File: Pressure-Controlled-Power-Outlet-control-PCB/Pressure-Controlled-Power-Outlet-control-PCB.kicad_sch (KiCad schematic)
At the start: 56 parts, among them J1 pressure sensor, J10 Conn_01x02_Pin, J2 1017514, J3 I2C0 Connector, J4 SPI1 Connector, J5 FanA 5V/12V, J6 FanB 5V/12V, J7 Conn_01x02_Pin, K1 T9GV5L24-24, K2 T9GV5L24-24, M1 Fan_4pin, M2 Fan_4pin, Q1 2N3906, Q2 IRF540N, Q3 IRF540N, Q4 2N3906, Q5 2N3904, Q6 2N3904, Q7 2N3904, Q8 2N3904, U1 Pico, U2 LM324, U3 LD1085V50, U4 LM1085-12

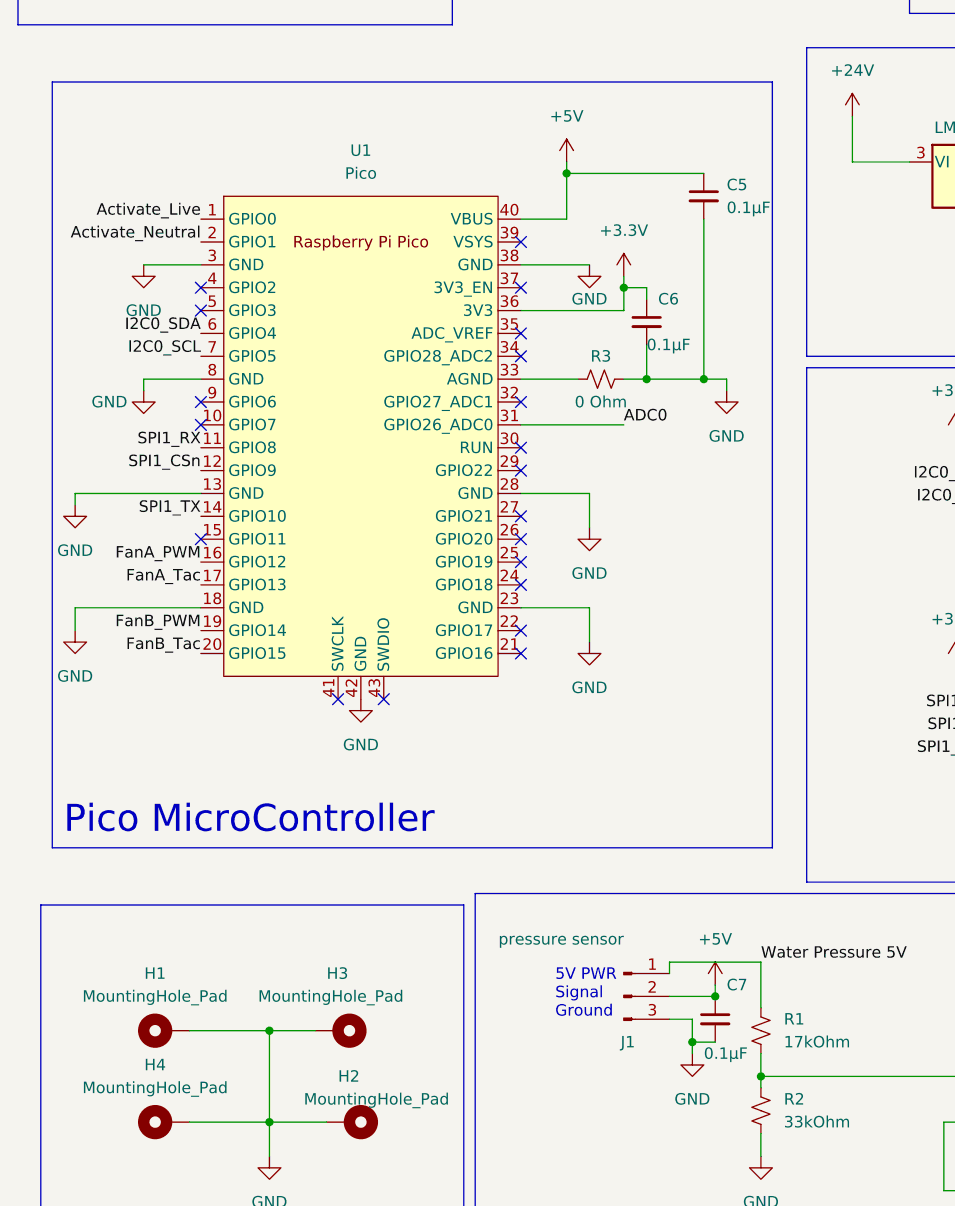
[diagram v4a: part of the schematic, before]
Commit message: created new updated PCB design that will fit the mount of the case
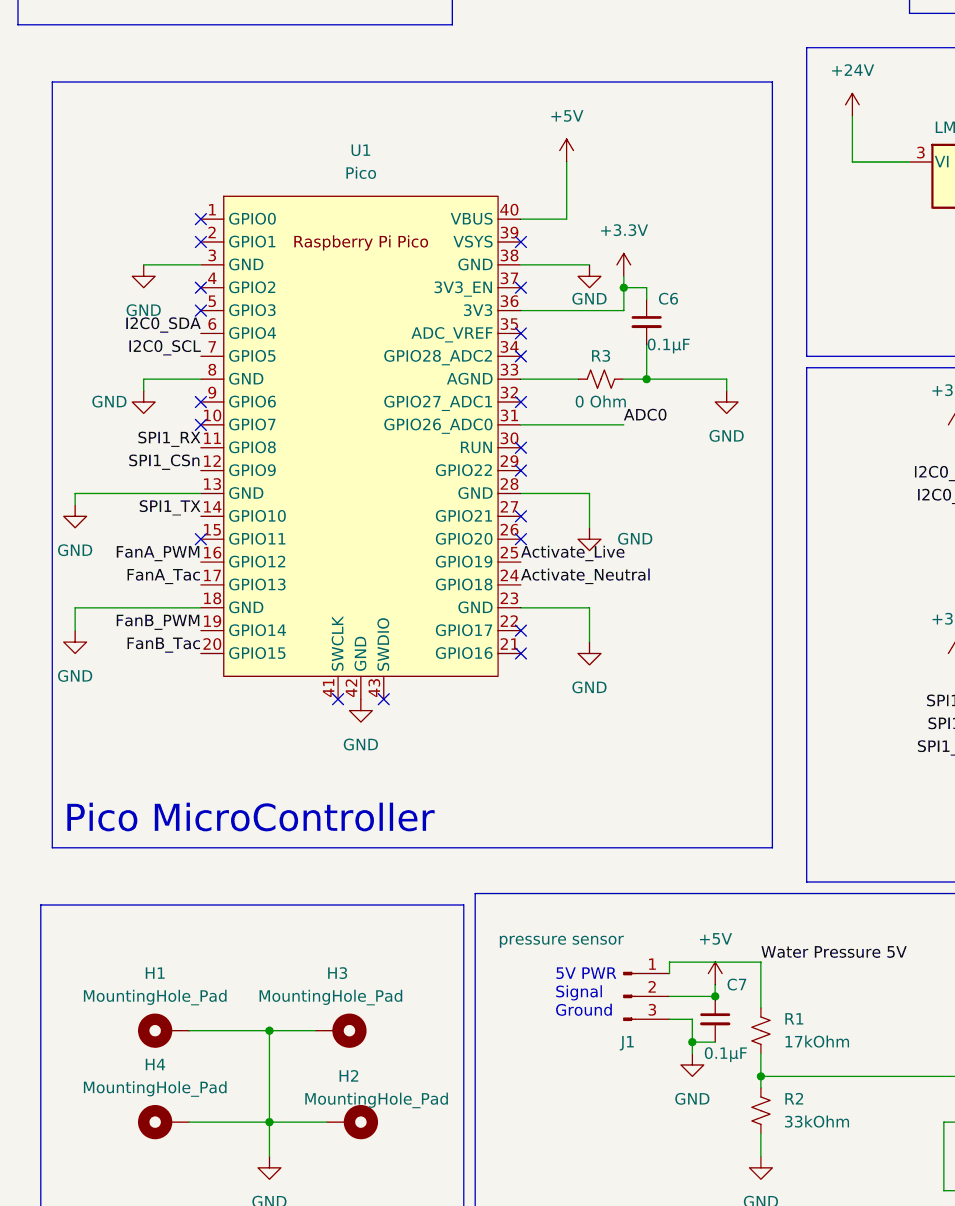
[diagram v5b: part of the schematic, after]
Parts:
- removed C5: 0.1µF, Capacitor_THT:C_Rect_L7.2mm_W2.5mm_P5.00mm_FKS2_FKP2_MKS2_MKP2, symbol Device:C_Small
- H1, H2, H3, H4: footprint MountingHole:MountingHole_4.3mm_M4_Pad -> MountingHole:MountingHole_3.2mm_M3_ISO7380_Pad
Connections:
- net Activate_Live: now also U1.25 (GPIO19); no longer U1.1 (GPIO0)
- net Activate_Neutral: now also U1.24 (GPIO18); no longer U1.2 (GPIO1)
- net Water Pressure 5V: now also R1.2; no longer R1.1
- net at R2.1, U2.3 (+): now also R1.1; no longer R1.2
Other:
- moved on the sheet: R1
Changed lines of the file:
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@@
   (junction (at 69.85 30.48) (diameter 0) (color 0 0 0 0)
   )
-  (junction (at 95.25 176.53) (diameter 0) (color 0 0 0 0)
-  )
   (junction (at 40.64 171.45) (diameter 0) (color 0 0 0 0)
   )
@@
   (junction (at 228.6 125.73) (diameter 0) (color 0 0 0 0)
   )
-  (junction (at 73.66 76.2) (diameter 0) (color 0 0 0 0)
-  )
   (junction (at 157.48 39.37) (diameter 0) (color 0 0 0 0)
   )
@@
   (junction (at 87.63 172.72) (diameter 0) (color 0 0 0 0)
   )
+  (junction (at 95.25 176.53) (diameter 0) (color 0 0 0 0)
+  )
   (junction (at 90.17 167.64) (diameter 0) (color 0 0 0 0)
   )
@@
   (junction (at 232.41 115.57) (diameter 0) (color 0 0 0 0)
   )
-  (junction (at 88.9 99.06) (diameter 0) (color 0 0 0 0)
-  )
   (junction (at 99.06 30.48) (diameter 0) (color 0 0 0 0)
   )
@@
   (no_connect (at 68.58 127))
   (no_connect (at 68.58 114.3))
+  (no_connect (at 33.02 81.28))
   (no_connect (at 247.65 88.9))
   (no_connect (at 68.58 83.82))
@@
   (no_connect (at 68.58 88.9))
   (no_connect (at 280.67 91.44))
-  (no_connect (at 68.58 119.38))
   (no_connect (at 68.58 116.84))
   (no_connect (at 68.58 106.68))
   (no_connect (at 246.38 119.38))
-  (no_connect (at 68.58 121.92))
   (no_connect (at 68.58 96.52))
   (no_connect (at 33.02 101.6))
+  (no_connect (at 33.02 83.82))
   (wire (pts (xy 48.26 49.53) (xy 48.26 50.8))
     (stroke (width 0) (type default))
@@
     (stroke (width 0) (type default))
   )
-  (wire (pts (xy 88.9 99.06) (xy 91.44 99.06))
+  (wire (pts (xy 82.55 99.06) (xy 91.44 99.06))
     (stroke (width 0) (type default))
   )
@@
     (stroke (width 0) (type default))
   )
-  (wire (pts (xy 88.9 81.28) (xy 88.9 99.06))
-    (stroke (width 0) (type default))
-  )
   (wire (pts (xy 99.06 40.64) (xy 85.09 40.64))
     (stroke (width 0) (type default))
@@
     (stroke (width 0) (type default))
   )
+  (wire (pts (xy 95.25 163.83) (xy 95.25 168.91))
+    (stroke (width 0) (type default))
+  )
   (wire (pts (xy 264.16 25.4) (xy 264.16 24.13))
     (stroke (width 0) (type default))
@@
     (stroke (width 0) (type default))
   )
-  (wire (pts (xy 73.66 74.93) (xy 73.66 76.2))
+  (wire (pts (xy 73.66 74.93) (xy 73.66 81.28))
     (stroke (width 0) (type default))
   )
@@
     (stroke (width 0) (type default))
   )
-  (wire (pts (xy 73.66 76.2) (xy 88.9 76.2))
-    (stroke (width 0) (type default))
-  )
-  (wire (pts (xy 95.25 163.83) (xy 95.25 168.91))
-    (stroke (width 0) (type default))
-  )
   (wire (pts (xy 99.06 30.48) (xy 92.71 30.48))
     (stroke (width 0) (type default))
@@
     (stroke (width 0) (type default))
   )
-  (wire (pts (xy 82.55 99.06) (xy 88.9 99.06))
-    (stroke (width 0) (type default))
-  )
   (wire (pts (xy 19.05 124.46) (xy 33.02 124.46))
     (stroke (width 0) (type default))
@@
     (stroke (width 0) (type default))
   )
-  (wire (pts (xy 95.25 173.99) (xy 95.25 176.53))
-    (stroke (width 0) (type default))
-  )
   (wire (pts (xy 228.6 153.67) (xy 228.6 157.48))
     (stroke (width 0) (type default))
@@
     (stroke (width 0) (type default))
   )
-  (wire (pts (xy 73.66 76.2) (xy 73.66 81.28))
-    (stroke (width 0) (type default))
-  )
   (wire (pts (xy 243.84 93.98) (xy 243.84 90.17))
     (stroke (width 0) (type default))
@@
     (stroke (width 0) (type default))
   )
+  (wire (pts (xy 95.25 173.99) (xy 95.25 176.53))
+    (stroke (width 0) (type default))
+  )
   (wire (pts (xy 179.07 44.45) (xy 179.07 48.26))
     (stroke (width 0) (type default))
@@
     (effects (font (size 3 3)) (justify left bottom))
   )
+  (label "Activate_Live" (at 68.58 119.38 0) (fields_autoplaced)
+    (effects (font (size 1.27 1.27)) (justify left bottom))
+  )
   (label "I2C0_SDA" (at 120.65 110.49 180) (fields_autoplaced)
     (effects (font (size 1.27 1.27)) (justify right bottom))
@@
     (effects (font (size 1.27 1.27)) (justify right bottom))
   )
-  (label "Activate_Neutral" (at 33.02 83.82 180) (fields_autoplaced)
-    (effects (font (size 1.27 1.27)) (justify right bottom))
-  )
   (label "FanA_Power" (at 179.07 29.21 180) (fields_autoplaced)
     (effects (font (size 1.27 1.27)) (justify right bottom))
@@
     (effects (font (size 1.27 1.27)) (justify right bottom))
   )
+  (label "Activate_Neutral" (at 68.58 121.92 0) (fields_autoplaced)
+    (effects (font (size 1.27 1.27)) (justify left bottom))
+  )
   (label "ADC0" (at 139.7 179.07 0) (fields_autoplaced)
     (effects (font (size 1.27 1.27)) (justify left bottom))
@@
     (effects (font (size 1.27 1.27)) (justify right bottom))
   )
-  (label "Activate_Live" (at 33.02 81.28 180) (fields_autoplaced)
-    (effects (font (size 1.27 1.27)) (justify right bottom))
-  )
   (label "SPI1_RX" (at 33.02 106.68 180) (fields_autoplaced)
     (effects (font (size 1.27 1.27)) (justify right bottom))
@@
       (effects (font (size 1.27 1.27)))
     )
-    (property "Footprint" "MountingHole:MountingHole_4.3mm_M4_Pad" (at 29.21 171.45 0)
+    (property "Footprint" "MountingHole:MountingHole_3.2mm_M3_ISO7380_Pad" (at 29.21 171.45 0)
       (effects (font (size 1.27 1.27)) hide)
     )
@@
       (effects (font (size 1.27 1.27)) (justify left))
     )
-    (property "Footprint" "MountingHole:MountingHole_4.3mm_M4_Pad" (at 48.26 171.45 0)
+    (property "Footprint" "MountingHole:MountingHole_3.2mm_M3_ISO7380_Pad" (at 48.26 171.45 0)
       (effects (font (size 1.27 1.27)) hide)
     )
@@
     )
   )
-  (symbol (lib_id "Device:R_Small_US") (at 95.25 171.45 0) (unit 1)
+  (symbol (lib_id "Device:R_Small_US") (at 95.25 171.45 180) (unit 1)
     (in_bom yes) (on_board yes) (dnp no) (fields_autoplaced)
     (property "Reference" "R1" (at 97.79 170.18 0)
-      (effects (font (size 1.27 1.27)) (justify left))
+      (effects (font (size 1.27 1.27)) (justify right))
     )
     (property "Value" "17kOhm" (at 97.79 172.72 0)
-      (effects (font (size 1.27 1.27)) (justify left))
+      (effects (font (size 1.27 1.27)) (justify right))
     )
     (property "Footprint" "Resistor_THT:R_Axial_DIN0207_L6.3mm_D2.5mm_P2.54mm_Vertical" (at 95.25 171.45 0)
@@
       (effects (font (size 1.27 1.27)) (justify left))
     )
-    (property "Footprint" "MountingHole:MountingHole_4.3mm_M4_Pad" (at 49.53 181.61 0)
+    (property "Footprint" "MountingHole:MountingHole_3.2mm_M3_ISO7380_Pad" (at 49.53 181.61 0)
       (effects (font (size 1.27 1.27)) hide)
     )
@@
   )
   (symbol (lib_id "power:GND") (at 76.2 115.57 0) (unit 1)
-    (in_bom yes) (on_board yes) (dnp no) (fields_autoplaced)
+    (in_bom yes) (on_board yes) (dnp no)
     (property "Reference" "#PWR07" (at 76.2 121.92 0)
       (effects (font (size 1.27 1.27)) hide)
     )
-    (property "Value" "GND" (at 76.2 120.65 0)
+    (property "Value" "GND" (at 81.28 116.84 0)
       (effects (font (size 1.27 1.27)))
     )
@@
     )
   )
-  (symbol (lib_id "Device:C_Small") (at 88.9 78.74 0) (unit 1)
-    (in_bom yes) (on_board yes) (dnp no) (fields_autoplaced)
-    (property "Reference" "C5" (at 91.44 77.4763 0)
-      (effects (font (size 1.27 1.27)) (justify left))
-    )
-    (property "Value" "0.1µF" (at 91.44 80.0163 0)
-      (effects (font (size 1.27 1.27)) (justify left))
-    )
-    (property "Footprint" "Capacitor_THT:C_Rect_L7.2mm_W2.5mm_P5.00mm_FKS2_FKP2_MKS2_MKP2" (at 88.9 78.74 0)
-      (effects (font (size 1.27 1.27)) hide)
-    )
-    (property "Datasheet" "~" (at 88.9 78.74 0)
-      (effects (font (size 1.27 1.27)) hide)
-    )
-    (pin "1")
-    (pin "2")
-    (instances
-      (project "Pressure-Controlled-Power-Outlet-control-PCB"
-        (path "/db34d92e-5e84-4492-8b7e-15d9a09f9218"
-          (reference "C5") (unit 1)
-        )
-      )
-    )
-  )
   (symbol (lib_id "power:GND") (at 237.49 52.07 0) (unit 1)
     (in_bom yes) (on_board yes) (dnp no) (fields_autoplaced)
@@
       (effects (font (size 1.27 1.27)))
     )
-    (property "Footprint" "MountingHole:MountingHole_4.3mm_M4_Pad" (at 29.21 181.61 0)
+    (property "Footprint" "MountingHole:MountingHole_3.2mm_M3_ISO7380_Pad" (at 29.21 181.61 0)
       (effects (font (size 1.27 1.27)) hide)
     )

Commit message: moved some componets
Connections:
- net +5V: now also Q1.1 (E), Q4.1 (E); no longer Q1.3 (C), Q4.3 (C)
- net at R5.1, R6.2: now also Q1.3 (C); no longer Q1.1 (E)
- net at R4.1, R7.2: now also Q4.3 (C); no longer Q4.1 (E)
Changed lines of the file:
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@@
-    )
-  )
-  (symbol (lib_id "Transistor_BJT:2N3906") (at 191.77 134.62 0) (unit 1)
-    (in_bom yes) (on_board yes) (dnp no) (fields_autoplaced)
-    (property "Reference" "Q1" (at 196.85 133.35 0)
-      (effects (font (size 1.27 1.27)) (justify left))
-    )
-    (property "Value" "2N3906" (at 196.85 135.89 0)
-      (effects (font (size 1.27 1.27)) (justify left))
-    )
-    (property "Footprint" "Package_TO_SOT_THT:TO-92_Inline" (at 196.85 136.525 0)
-      (effects (font (size 1.27 1.27) italic) (justify left) hide)
-    )
-    (property "Datasheet" "https://www.onsemi.com/pub/Collateral/2N3906-D.PDF" (at 191.77 134.62 0)
-      (effects (font (size 1.27 1.27)) (justify left) hide)
-    )
-    (pin "1")
-    (pin "3")
-    (pin "2")
-    (instances
-      (project "Pressure-Controlled-Power-Outlet-control-PCB"
-        (path "/db34d92e-5e84-4492-8b7e-15d9a09f9218"
-          (reference "Q1") (unit 1)
-        )
-      )
     )
   )
@@
         (path "/db34d92e-5e84-4492-8b7e-15d9a09f9218"
           (reference "#PWR058") (unit 1)
-        )
-      )
-    )
-  )
-  (symbol (lib_id "Transistor_BJT:2N3906") (at 193.04 107.95 0) (unit 1)
-    (in_bom yes) (on_board yes) (dnp no) (fields_autoplaced)
-    (property "Reference" "Q4" (at 198.12 106.68 0)
-      (effects (font (size 1.27 1.27)) (justify left))
-    )
-    (property "Value" "2N3906" (at 198.12 109.22 0)
-      (effects (font (size 1.27 1.27)) (justify left))
-    )
-    (property "Footprint" "Package_TO_SOT_THT:TO-92_Inline" (at 198.12 109.855 0)
-      (effects (font (size 1.27 1.27) italic) (justify left) hide)
-    )
-    (property "Datasheet" "https://www.onsemi.com/pub/Collateral/2N3906-D.PDF" (at 193.04 107.95 0)
-      (effects (font (size 1.27 1.27)) (justify left) hide)
-    )
-    (pin "1")
-    (pin "3")
-    (pin "2")
-    (instances
-      (project "Pressure-Controlled-Power-Outlet-control-PCB"
-        (path "/db34d92e-5e84-4492-8b7e-15d9a09f9218"
-          (reference "Q4") (unit 1)
         )
       )
@@
     )
   )
+  (symbol (lib_id "Transistor_BJT:2N3906") (at 191.77 134.62 0) (mirror x) (unit 1)
+    (in_bom yes) (on_board yes) (dnp no)
+    (property "Reference" "Q1" (at 196.85 135.89 0)
+      (effects (font (size 1.27 1.27)) (justify left))
+    )
+    (property "Value" "2N3906" (at 196.85 133.35 0)
+      (effects (font (size 1.27 1.27)) (justify left))
+    )
+    (property "Footprint" "Package_TO_SOT_THT:TO-92_Inline" (at 196.85 132.715 0)
+      (effects (font (size 1.27 1.27) italic) (justify left) hide)
+    )
+    (property "Datasheet" "https://www.onsemi.com/pub/Collateral/2N3906-D.PDF" (at 191.77 134.62 0)
+      (effects (font (size 1.27 1.27)) (justify left) hide)
+    )
+    (pin "1")
+    (pin "3")
+    (pin "2")
+    (instances
+      (project "Pressure-Controlled-Power-Outlet-control-PCB"
+        (path "/db34d92e-5e84-4492-8b7e-15d9a09f9218"
+          (reference "Q1") (unit 1)
+        )
+      )
+    )
+  )
   (symbol (lib_id "power:+5V") (at 195.58 100.33 0) (unit 1)
     (in_bom yes) (on_board yes) (dnp no) (fields_autoplaced)
@@
         )
       )
+    )
+  )
+  (symbol (lib_id "Transistor_BJT:2N3906") (at 193.04 107.95 0) (mirror x) (unit 1)
+    (in_bom yes) (on_board yes) (dnp no)
+    (property "Reference" "Q4" (at 198.12 109.22 0)
+      (effects (font (size 1.27 1.27)) (justify left))
+    )
+    (property "Value" "2N3906" (at 198.12 106.68 0)
+      (effects (font (size 1.27 1.27)) (justify left))
+    )
+    (property "Footprint" "Package_TO_SOT_THT:TO-92_Inline" (at 198.12 106.045 0)
+      (effects (font (size 1.27 1.27) italic) (justify left) hide)
+    )
+    (property "Datasheet" "https://www.onsemi.com/pub/Collateral/2N3906-D.PDF" (at 193.04 107.95 0)
+      (effects (font (size 1.27 1.27)) (justify left) hide)
+    )
+    (pin "1")
+    (pin "3")
+    (pin "2")
+    (instances
+      (project "Pressure-Controlled-Power-Outlet-control-PCB"
+        (path "/db34d92e-5e84-4492-8b7e-15d9a09f9218"
+          (reference "Q4") (unit 1)
+        )
+      )
